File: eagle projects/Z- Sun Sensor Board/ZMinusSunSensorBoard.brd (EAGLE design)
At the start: 91 x 91 mm, 204 parts, among them J1 TE-1734829-2, U1 ADS7841E_2K5, U10 TSV991AILT, U11 TSV991AILT, U12 TSV991AILT, U13 ADS7841E_2K5, U14 TSV991AILT, U16 TSV991AILT, U17 TSV991AILT, U19 TSV991AILT, U2 ADS7841E_2K5, U21 TSV991AILT, U23 TSV991AILT, U25 ADS7841E_2K5, U26 TSV991AILT, U27 ADS7841E_2K5, U29 TSV991AILT, U3 TSV991AILT, U4 LM20BIM7X_NOPB, U5 LM20BIM7X_NOPB, U6 TSV991AILT, U8 TSV991AILT, U9 TSV991AILT

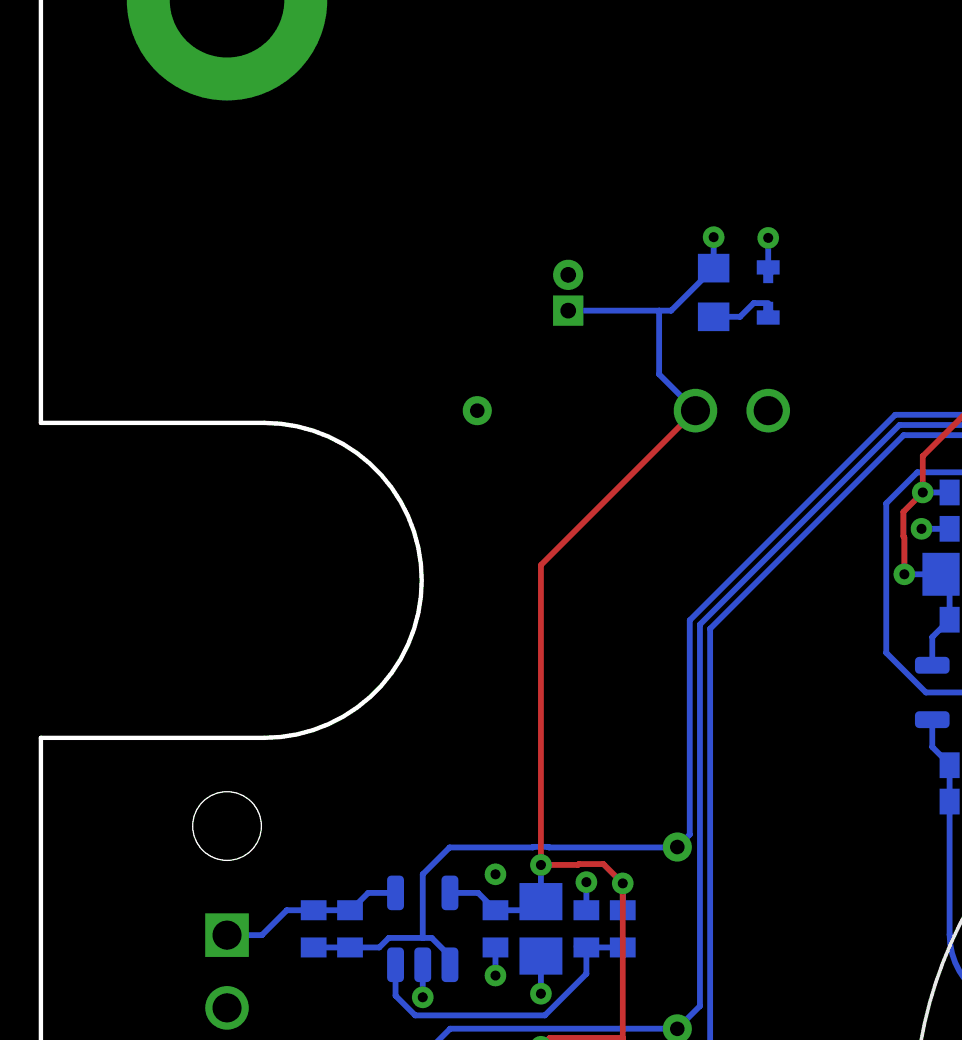
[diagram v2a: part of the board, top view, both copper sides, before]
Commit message: Moved text
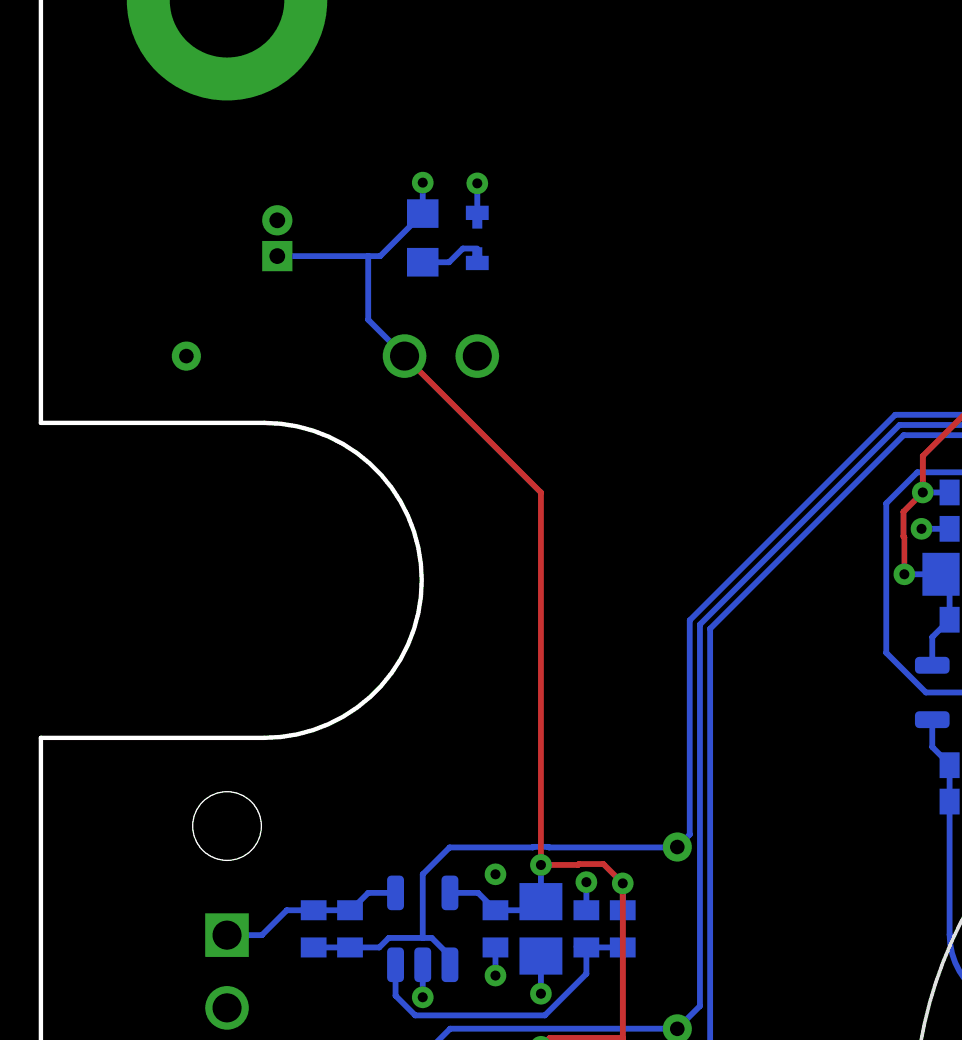
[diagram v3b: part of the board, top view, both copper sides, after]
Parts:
- moved R11 10.3 mm to (13.3, 76.2)
- moved TP4 10.3 mm to (5.08, 72.1)
- moved J1 10.3 mm to (8.26, 75.6)
- moved J3 10.3 mm to (14.0, 72.1)
- moved LED1 10.3 mm to (15.2, 76.2)
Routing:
- net +3V3: track 487.3 -> 488.9 mm
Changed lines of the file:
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@@
 <rectangle x1="23.8633" y1="31.8389" x2="24.4729" y2="31.8643" layer="21"/>
 <rectangle x1="24.0157" y1="31.8643" x2="24.2697" y2="31.8897" layer="21"/>
-<text x="27.94" y="71.4375" size="1.016" layer="22" rot="MR270">GND</text>
-<text x="21.2725" y="71.4375" size="1.016" layer="22" rot="MR270">+3V3</text>
+<text x="17.78" y="73.3425" size="1.016" layer="22" rot="MR270">GND</text>
+<text x="11.1125" y="73.3425" size="1.016" layer="22" rot="MR270">+3V3</text>
 <rectangle x1="32.9819" y1="13.5001" x2="33.3375" y2="13.5255" layer="22" rot="R180"/>
 <rectangle x1="28.6639" y1="13.5001" x2="29.0195" y2="13.5255" layer="22" rot="R180"/>
@@
 <attribute name="NAME" x="73.787" y="67.5005" size="1.016" layer="26" ratio="10" rot="MR180"/>
 </element>
-<element name="TP4" library="my_library" library_urn="urn:adsk.eagle:library:22876504" package="TP_P76H50" package3d_urn="urn:adsk.eagle:package:24605432/3" value="TESTPOINT" x="15.24" y="70.1675" smashed="yes" rot="MR270">
-<attribute name="NAME" x="16.3195" y="70.6755" size="1.016" layer="26" ratio="10" rot="MR180"/>
+<element name="TP4" library="my_library" library_urn="urn:adsk.eagle:library:22876504" package="TP_P76H50" package3d_urn="urn:adsk.eagle:package:24605432/3" value="TESTPOINT" x="5.08" y="72.0725" smashed="yes" rot="MR270">
+<attribute name="NAME" x="6.1595" y="72.5805" size="1.016" layer="26" ratio="10" rot="MR180"/>
 </element>
 <element name="U1" library="my_library" library_urn="urn:adsk.eagle:library:22876504" package="DBQ16" package3d_urn="urn:adsk.eagle:package:23087509/6" value="ADS7841E_2K5" x="68.58" y="75.565" smashed="yes" rot="MR180">
@@
 <element name="U$4" library="my_library" library_urn="urn:adsk.eagle:library:22876504" package="PHOTODIODE_SILK" value="" x="30.41514375" y="36.305059375" locked="yes" smashed="yes" rot="R300"/>
 <element name="U$5" library="my_library" library_urn="urn:adsk.eagle:library:22876504" package="PHOTODIODE_SILK" value="" x="60.966615625" y="36.494215625" locked="yes" smashed="yes" rot="R60"/>
-<element name="J1" library="my_library" library_urn="urn:adsk.eagle:library:22876504" package="TE-1734829-2" package3d_urn="urn:adsk.eagle:package:27602902/2" value="TE-1734829-2" x="18.415" y="73.66" smashed="yes" rot="MR270">
-<attribute name="NAME" x="19.685" y="77.47" size="1.27" layer="26" rot="MR180"/>
+<element name="J1" library="my_library" library_urn="urn:adsk.eagle:library:22876504" package="TE-1734829-2" package3d_urn="urn:adsk.eagle:package:27602902/2" value="TE-1734829-2" x="8.255" y="75.565" smashed="yes" rot="MR270">
+<attribute name="NAME" x="9.525" y="79.375" size="1.27" layer="26" rot="MR180"/>
 </element>
-<element name="J3" library="my_library" library_urn="urn:adsk.eagle:library:22876504" package="1X02" package3d_urn="urn:adsk.eagle:package:24527019/1" value="" x="24.13" y="70.1675" smashed="yes" rot="MR180">
-<attribute name="NAME" x="26.4287" y="67.2338" size="1.27" layer="26" ratio="10" rot="MR0"/>
-<attribute name="VALUE" x="21.59" y="73.3425" size="1.27" layer="28" rot="MR180"/>
-</element>
-<element name="R11" library="rcl" library_urn="urn:adsk.eagle:library:334" package="R0603" package3d_urn="urn:adsk.eagle:package:23555/3" value="" x="23.495" y="74.295" smashed="yes" rot="MR90">
-<attribute name="NAME" x="21.2725" y="73.025" size="1.27" layer="26" rot="MR90"/>
-<attribute name="POPULARITY" value="77" x="23.495" y="74.295" size="1.778" layer="28" rot="MR90" display="off"/>
-<attribute name="SPICEPREFIX" value="R" x="23.495" y="74.295" size="1.778" layer="28" rot="MR90" display="off"/>
-<attribute name="VALUE" x="21.59" y="73.66" size="1.27" layer="28" rot="MR90"/>
-</element>
-<element name="LED1" library="led" library_urn="urn:adsk.eagle:library:259" package="CHIPLED-0603-TTW" package3d_urn="urn:adsk.eagle:package:15824/1" value="" x="25.4" y="74.295" smashed="yes" rot="MR0">
-<attribute name="POPULARITY" value="0" x="25.4" y="74.295" size="1.778" layer="28" rot="MR0" display="off"/>
-<attribute name="VALUE" x="23.495" y="73.025" size="1.27" layer="28" rot="MR90"/>
+<element name="J3" library="my_library" library_urn="urn:adsk.eagle:library:22876504" package="1X02" package3d_urn="urn:adsk.eagle:package:24527019/1" value="" x="13.97" y="72.0725" smashed="yes" rot="MR180">
+<attribute name="NAME" x="16.2687" y="69.1388" size="1.27" layer="26" ratio="10" rot="MR0"/>
+<attribute name="VALUE" x="11.43" y="75.2475" size="1.27" layer="28" rot="MR180"/>
+</element>
+<element name="R11" library="rcl" library_urn="urn:adsk.eagle:library:334" package="R0603" package3d_urn="urn:adsk.eagle:package:23555/3" value="" x="13.335" y="76.2" smashed="yes" rot="MR90">
+<attribute name="NAME" x="11.1125" y="74.93" size="1.27" layer="26" rot="MR90"/>
+<attribute name="POPULARITY" value="77" x="13.335" y="76.2" size="1.778" layer="28" rot="MR90" display="off"/>
+<attribute name="SPICEPREFIX" value="R" x="13.335" y="76.2" size="1.778" layer="28" rot="MR90" display="off"/>
+<attribute name="VALUE" x="11.43" y="75.565" size="1.27" layer="28" rot="MR90"/>
+</element>
+<element name="LED1" library="led" library_urn="urn:adsk.eagle:library:259" package="CHIPLED-0603-TTW" package3d_urn="urn:adsk.eagle:package:15824/1" value="" x="15.24" y="76.2" smashed="yes" rot="MR0">
+<attribute name="POPULARITY" value="0" x="15.24" y="76.2" size="1.778" layer="28" rot="MR0" display="off"/>
+<attribute name="VALUE" x="13.335" y="74.93" size="1.27" layer="28" rot="MR90"/>
 </element>
 <element name="U5" library="my_library" library_urn="urn:adsk.eagle:library:22876504" package="SOT23-5P65_210X110L40X22N_LM20" package3d_urn="urn:adsk.eagle:package:23087469/2" value="LM20BIM7X_NOPB" x="58.42" y="23.495" smashed="yes" rot="R90">
@@
 <wire x1="15.875" y1="40.02" x2="17.16" y2="40.02" width="0.2032" layer="16"/>
 <wire x1="17.16" y1="40.02" x2="17.4625" y2="40.3225" width="0.2032" layer="16"/>
-<wire x1="23.495" y1="75.145" x2="23.495" y2="76.2256" width="0.2032" layer="16"/>
-<via x="23.495" y="76.2256" extent="1-16" drill="0.35"/>
+<wire x1="13.335" y1="77.05" x2="13.335" y2="78.1306" width="0.2032" layer="16"/>
+<via x="13.335" y="78.1306" extent="1-16" drill="0.35"/>
 <contactref element="J2" pad="10"/>
 <contactref element="U5" pad="4"/>
@@
 <wire x1="54.9275" y1="24.145" x2="54.9275" y2="25.0825" width="0.2032" layer="16"/>
 <via x="54.9275" y="25.0825" extent="1-16" drill="0.35"/>
-<wire x1="23.495" y1="75.145" x2="22.01" y2="73.66" width="0.2032" layer="16"/>
-<wire x1="22.01" y1="73.66" x2="21.59" y2="73.66" width="0.2032" layer="16"/>
-<wire x1="21.59" y1="73.66" x2="18.415" y2="73.66" width="0.2032" layer="16"/>
-<wire x1="21.59" y1="73.66" x2="21.59" y2="71.4375" width="0.2032" layer="16"/>
-<wire x1="21.59" y1="71.4375" x2="22.86" y2="70.1675" width="0.2032" layer="16"/>
-<wire x1="17.4625" y1="64.77" x2="22.86" y2="70.1675" width="0.2032" layer="1"/>
+<wire x1="13.335" y1="77.05" x2="11.85" y2="75.565" width="0.2032" layer="16"/>
+<wire x1="11.85" y1="75.565" x2="11.43" y2="75.565" width="0.2032" layer="16"/>
+<wire x1="11.43" y1="75.565" x2="8.255" y2="75.565" width="0.2032" layer="16"/>
+<wire x1="11.43" y1="75.565" x2="11.43" y2="73.3425" width="0.2032" layer="16"/>
+<wire x1="11.43" y1="73.3425" x2="12.7" y2="72.0725" width="0.2032" layer="16"/>
+<wire x1="17.4625" y1="67.31" x2="12.7" y2="72.0725" width="0.2032" layer="1"/>
 <wire x1="17.4625" y1="54.3006" x2="18.75593125" y2="54.3006" width="0.2032" layer="1"/>
 <wire x1="18.75593125" y1="54.3006" x2="18.78813125" y2="54.3328" width="0.2032" layer="1"/>
@@
 <wire x1="17.4625" y1="41.6006" x2="17.7719" y2="41.91" width="0.2032" layer="1"/>
 <wire x1="17.7719" y1="41.91" x2="20.32" y2="41.91" width="0.2032" layer="1"/>
-<wire x1="17.4625" y1="54.3006" x2="17.4625" y2="64.77" width="0.2032" layer="1"/>
+<wire x1="17.4625" y1="54.3006" x2="17.4625" y2="67.31" width="0.2032" layer="1"/>
 <wire x1="20.32" y1="40.9575" x2="22.5425" y2="40.9575" width="0.2032" layer="1"/>
 <wire x1="33.02" y1="30.48" x2="33.02" y2="22.86" width="0.2032" layer="1"/>
@@
 <via x="75.565" y="69.215" extent="1-16" drill="0.35"/>
 <via x="75.2475" y="52.3875" extent="1-16" drill="0.35"/>
-<via x="25.4" y="76.2" extent="1-16" drill="0.35"/>
+<via x="15.24" y="78.105" extent="1-16" drill="0.35"/>
 <contactref element="R25" pad="2"/>
 <wire x1="87.495" y1="71.755" x2="88.5825" y2="71.755" width="0.2032" layer="16"/>
 <via x="88.5825" y="71.755" extent="1-16" drill="0.35"/>
-<wire x1="25.4" y1="74.795" x2="25.4" y2="76.2" width="0.2032" layer="16"/>
+<wire x1="15.24" y1="76.7" x2="15.24" y2="78.105" width="0.2032" layer="16"/>
 <wire x1="57.52" y1="22.845" x2="56.2125" y2="22.845" width="0.2032" layer="1"/>
 <wire x1="56.2125" y1="22.845" x2="56.1975" y2="22.86" width="0.2032" layer="1"/>
@@
 </signal>
 <signal name="N$21">
-<wire x1="23.495" y1="73.445" x2="23.71" y2="73.66" width="0.2032" layer="16"/>
+<wire x1="13.335" y1="75.35" x2="13.55" y2="75.565" width="0.2032" layer="16"/>
 <contactref element="R11" pad="1"/>
 <contactref element="LED1" pad="A@1"/>
-<wire x1="24.8947875" y1="73.924" x2="25.4" y2="73.924" width="0.2032" layer="16"/>
-<wire x1="23.495" y1="73.445" x2="24.4157875" y2="73.445" width="0.2032" layer="16"/>
-<wire x1="24.4157875" y1="73.445" x2="24.8947875" y2="73.924" width="0.2032" layer="16"/>
-<wire x1="25.4" y1="73.924" x2="25.4" y2="73.795" width="0" layer="19" extent="16-16"/>
+<wire x1="14.7347875" y1="75.829" x2="15.24" y2="75.829" width="0.2032" layer="16"/>
+<wire x1="13.335" y1="75.35" x2="14.2557875" y2="75.35" width="0.2032" layer="16"/>
+<wire x1="14.2557875" y1="75.35" x2="14.7347875" y2="75.829" width="0.2032" layer="16"/>
+<wire x1="15.24" y1="75.829" x2="15.24" y2="75.7" width="0" layer="19" extent="16-16"/>
 </signal>
 <signal name="N$20">

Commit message: I thinks its done
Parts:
- JP2, JP4, JP5, JP6: device my_library:1X06_MTG_HOLES -> my_library:2X03_MTG_HOLES
- LED1: device led:CHIPLED-0603-TTW -> led:CHIP-LED0603
- moved TP1 5.71 mm to (59.1, 65.7)
- moved U$3 3.55 mm to (46.0, 66.7)
- moved TP3 3.38 mm to (50.2, 64.8)
- moved C100 2.62 mm to (20.0, 38.7)
- moved C71 2.62 mm to (20.0, 51.4)
- moved C87 2.62 mm to (20.0, 45.1)
- moved R66 2.62 mm to (13.3, 51.4)
- moved R75 2.62 mm to (13.3, 45.1)
- moved R81 2.62 mm to (13.3, 38.7)
- moved TP23 2.62 mm to (24.8, 54.3)
- moved C101 2.62 mm to (18.4, 38.7)
- moved C103 2.62 mm to (12.1, 38.7)
- moved C82 2.62 mm to (18.4, 51.4)
- moved C83 2.62 mm to (12.1, 51.4)
- moved C88 2.62 mm to (18.4, 45.1)
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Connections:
- net GND: now also JP2.1, JP2.3, JP2.5, JP4.1, JP4.3, JP4.5, JP5.1, JP5.3, JP5.5, JP6.1, JP6.3, JP6.5, LED1.C; no longer JP2.2, JP2.4, JP2.6, JP4.2, JP4.4, JP4.6, JP5.2, JP5.4, JP5.6, JP6.2, JP6.4, JP6.6, LED1.C@1
- net N$21: now also LED1.A; no longer LED1.A@1
- net N$23: now also JP6.4; no longer JP6.3
- net N$29: now also JP6.6; no longer JP6.1
- net N$35: now also JP6.2; no longer JP6.5
- net N$37: now also JP5.2; no longer JP5.1
- net N$38: now also JP4.2; no longer JP4.1
- net N$44: now also JP4.4; no longer JP4.3
- net N$46: now also JP4.6; no longer JP4.5
- net N$49: now also JP2.2; no longer JP2.1
- net N$55: now also JP2.4; no longer JP2.3
- net N$57: now also JP2.6; no longer JP2.5
- net N$63: now also JP5.4; no longer JP5.3
- net N$65: now also JP5.6; no longer JP5.5
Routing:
- net +3V3: track 488.9 -> 497.4 mm
- net N$37: track 17.7 -> 12.5 mm
- net N$29: track 6.50 -> 9.67 mm
- net N$38: track 5.61 -> 8.14 mm
- net X-_120_DEGREES: track 40.2 -> 42.7 mm
- net X-_0_DEGREES: track 46.6 -> 49.0 mm
- net N$35: track 6.83 -> 8.89 mm
- net X-_240_DEGREES: track 22.4 -> 24.3 mm
- net N$27: track 18.0 -> 16.1 mm
- net N$63: track 18.1 -> 16.3 mm
- net N$46: track 7.68 -> 9.41 mm
- net N$49: track 6.95 -> 8.66 mm
- net Y-_120_DEGREES: track 79.6 -> 78.1 mm
- net Y-_240_DEGREES: track 74.2 -> 72.6 mm
- net N$42: track 16.8 -> 15.4 mm
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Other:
- board text added: "Z MINUS SUN SENSE BOARD REV B"
- board text removed: "Z MINUS SUN SENSE BOARD - REV A"
